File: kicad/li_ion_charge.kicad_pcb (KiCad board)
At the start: 2 copper layers, 18 parts, among them P101 USB_B, P102 CONN_01X02, P103 CONN_01X02, U101 MCP73834-FCI/UN

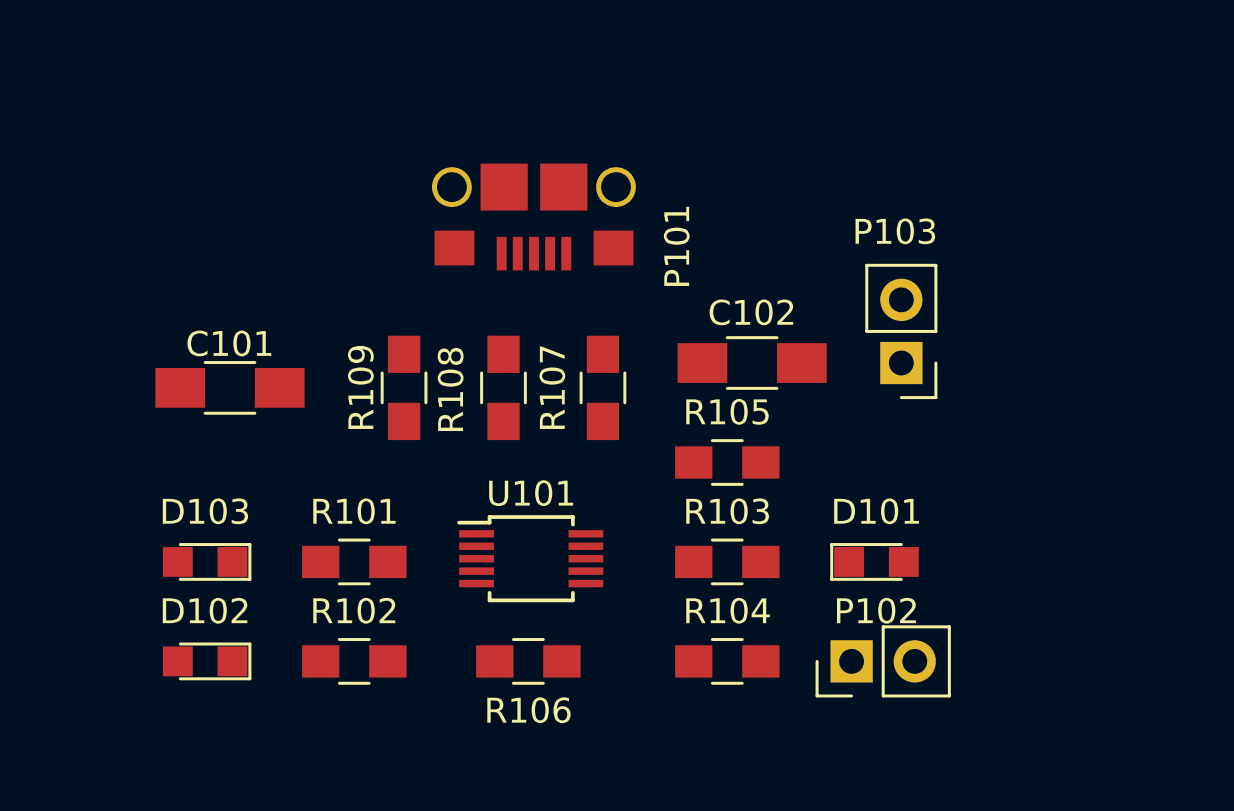
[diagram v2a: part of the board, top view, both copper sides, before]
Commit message: First iteration of adding power planes and initial traces. Still need to add osh-park defaults and address ERC errors
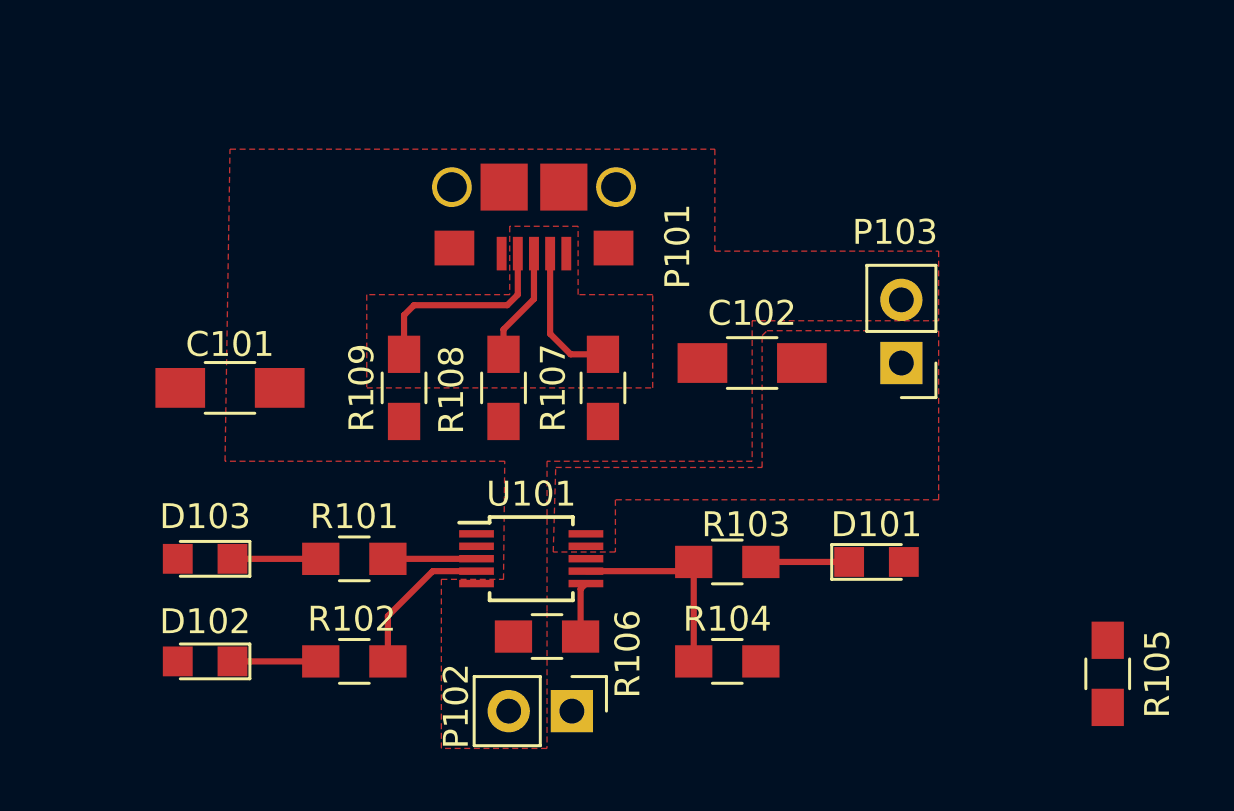
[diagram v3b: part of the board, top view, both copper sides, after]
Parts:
- moved R105 17.5 mm to (181.3, 107.5), turned to 270 degrees
- moved P102 11.4 mm to (159.8, 109.0), turned to 270 degrees
- moved R106 1.25 mm to (158.8, 106.0)
- moved D103 0.12 mm to (145.0, 102.9)
- moved R101 0.12 mm to (151.0, 102.9)
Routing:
- net /~TE: track 0.00 -> 8.49 mm
- net Net-(P101-Pad4): track 0.00 -> 8.14 mm
- net /Stat2: track 0.00 -> 6.14 mm
- net Net-(P101-Pad2): track 0.00 -> 5.69 mm
- net Net-(P101-Pad3): track 0.00 -> 4.56 mm
- net /Stat1: track 0.00 -> 3.57 mm
- net Net-(D103-Pad1): track 0.00 -> 3.55 mm
- net Net-(D102-Pad1): track 0.00 -> 3.55 mm
- net Net-(D101-Pad1): track 0.00 -> 3.55 mm
- net /Prog: track 0.00 -> 2.22 mm
- added copper zone on F.Cu, net /VBAT
- added copper zone on F.Cu, net GND
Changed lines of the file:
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@@
   (general
     (links 38)
-    (no_connects 38)
+    (no_connects 10)
     (area 0 0 0 0)
     (thickness 1.6)
     (drawings 0)
-    (tracks 2)
+    (tracks 26)
     (zones 0)
     (modules 18)
@@
     (last_trace_width 0.25)
     (trace_clearance 0.2)
-    (zone_clearance 0.508)
+    (zone_clearance 0.2032)
     (zone_45_only no)
     (trace_min 0.2)
@@
     (tags "LED led 0805 SMD smd SMT smt smdled SMDLED smtled SMTLED")
     (attr smd)
-    (fp_text reference D101 (at 0 -2) (layer F.SilkS)
+    (fp_text reference D101 (at 0 -1.5) (layer F.SilkS)
       (effects (font (size 1 1) (thickness 0.15)))
     )
@@
     (tags "LED led 0805 SMD smd SMT smt smdled SMDLED smtled SMTLED")
     (attr smd)
-    (fp_text reference D102 (at 0 2 180) (layer F.SilkS)
+    (fp_text reference D102 (at 0 1.6 180) (layer F.SilkS)
       (effects (font (size 1 1) (thickness 0.15)))
     )
@@
   )
   (module LEDs:LED_0805 (layer F.Cu)
-    (at 145 103 180)
+    (at 145 102.875 180)
     (descr "LED 0805 smd package")
     (tags "LED led 0805 SMD smd SMT smt smdled SMDLED smtled SMTLED")
     (attr smd)
-    (fp_text reference D103 (at 0 2 180) (layer F.SilkS)
+    (fp_text reference D103 (at 0 1.7 180) (layer F.SilkS)
       (effects (font (size 1 1) (thickness 0.15)))
     )
@@
   )
   (module Resistors_SMD:R_0805_HandSoldering (layer F.Cu)
-    (at 151 103 180)
+    (at 151 102.875 180)
     (descr "Resistor SMD 0805, hand soldering")
     (tags "resistor 0805")
     (attr smd)
-    (fp_text reference R101 (at 0 2 180) (layer F.SilkS)
+    (fp_text reference R101 (at 0 1.7 180) (layer F.SilkS)
       (effects (font (size 1 1) (thickness 0.15)))
     )
@@
     (tags "resistor 0805")
     (attr smd)
-    (fp_text reference R102 (at 0 2 180) (layer F.SilkS)
+    (fp_text reference R102 (at 0.1 1.7 180) (layer F.SilkS)
       (effects (font (size 1 1) (thickness 0.15)))
     )
@@
     (tags "resistor 0805")
     (attr smd)
-    (fp_text reference R103 (at 0 -2) (layer F.SilkS)
+    (fp_text reference R103 (at 0.75 -1.5) (layer F.SilkS)
       (effects (font (size 1 1) (thickness 0.15)))
     )
@@
     (tags "resistor 0805")
     (attr smd)
-    (fp_text reference R104 (at 0 -2) (layer F.SilkS)
+    (fp_text reference R104 (at 0 -1.7) (layer F.SilkS)
       (effects (font (size 1 1) (thickness 0.15)))
     )
@@
   )
   (module Resistors_SMD:R_0805_HandSoldering (layer F.Cu)
-    (at 166 99 180)
+    (at 181.3 107.5 270)
     (descr "Resistor SMD 0805, hand soldering")
     (tags "resistor 0805")
     (attr smd)
-    (fp_text reference R105 (at 0 2 180) (layer F.SilkS)
-      (effects (font (size 1 1) (thickness 0.15)))
-    )
-    (fp_text value 10k (at -4 0 180) (layer F.Fab)
-      (effects (font (size 1 1) (thickness 0.15)))
-    )
-    (fp_text user %R (at 0 -1.7 180) (layer F.Fab) hide
+    (fp_text reference R105 (at 0 -2 270) (layer F.SilkS)
+      (effects (font (size 1 1) (thickness 0.15)))
+    )
+    (fp_text value 10k (at -4 0 270) (layer F.Fab)
+      (effects (font (size 1 1) (thickness 0.15)))
+    )
+    (fp_text user %R (at 0 -1.7 270) (layer F.Fab) hide
       (effects (font (size 1 1) (thickness 0.15)))
     )
@@
     (fp_line (start 2.35 0.9) (end 2.35 -0.9) (layer F.CrtYd) (width 0.05))
     (fp_line (start 2.35 0.9) (end -2.35 0.9) (layer F.CrtYd) (width 0.05))
-    (pad 1 smd rect (at -1.35 0 180) (size 1.5 1.3) (layers F.Cu F.Paste F.Mask)
-      (net 1 GND))
-    (pad 2 smd rect (at 1.35 0 180) (size 1.5 1.3) (layers F.Cu F.Paste F.Mask)
+    (pad 1 smd rect (at -1.35 0 270) (size 1.5 1.3) (layers F.Cu F.Paste F.Mask)
+      (net 1 GND))
+    (pad 2 smd rect (at 1.35 0 270) (size 1.5 1.3) (layers F.Cu F.Paste F.Mask)
       (net 11 /Ther))
     (model Resistors_SMD.3dshapes/R_0805.wrl
@@
   )
   (module Resistors_SMD:R_0805_HandSoldering (layer F.Cu)
-    (at 158 107)
+    (at 158.75 106)
     (descr "Resistor SMD 0805, hand soldering")
     (tags "resistor 0805")
     (attr smd)
-    (fp_text reference R106 (at 0 2) (layer F.SilkS)
-      (effects (font (size 1 1) (thickness 0.15)))
-    )
-    (fp_text value 2k (at 3 0) (layer F.Fab)
+    (fp_text reference R106 (at 3.25 0.7 90) (layer F.SilkS)
+      (effects (font (size 1 1) (thickness 0.15)))
+    )
+    (fp_text value 2k (at 3 0) (layer F.Fab) hide
       (effects (font (size 1 1) (thickness 0.15)))
     )
@@
   )
   (module Pin_Headers:Pin_Header_Straight_1x02_Pitch2.54mm (layer F.Cu)
-    (at 171 107 90)
+    (at 159.75 109 270)
     (descr "Through hole straight pin header, 1x02, 2.54mm pitch, single row")
     (tags "Through hole pin header THT 1x02 2.54mm single row")
-    (fp_text reference P102 (at 2 1 180) (layer F.SilkS)
-      (effects (font (size 1 1) (thickness 0.15)))
-    )
-    (fp_text value CONN_01X02 (at 0 4.93 90) (layer F.Fab) hide
+    (fp_text reference P102 (at -0.2 4.65 270) (layer F.SilkS)
+      (effects (font (size 1 1) (thickness 0.15)))
+    )
+    (fp_text value CONN_01X02 (at 0 4.93 270) (layer F.Fab) hide
       (effects (font (size 1 1) (thickness 0.15)))
     )
@@
     (fp_line (start 1.6 4.1) (end 1.6 -1.6) (layer F.CrtYd) (width 0.05))
     (fp_line (start 1.6 -1.6) (end -1.6 -1.6) (layer F.CrtYd) (width 0.05))
-    (pad 1 thru_hole rect (at 0 0 90) (size 1.7 1.7) (drill 1) (layers *.Cu *.Mask)
+    (pad 1 thru_hole rect (at 0 0 270) (size 1.7 1.7) (drill 1) (layers *.Cu *.Mask)
       (net 9 /RESET))
-    (pad 2 thru_hole oval (at 0 2.54 90) (size 1.7 1.7) (drill 1) (layers *.Cu *.Mask)
+    (pad 2 thru_hole oval (at 0 2.54 270) (size 1.7 1.7) (drill 1) (layers *.Cu *.Mask)
       (net 1 GND))
     (model Pin_Headers.3dshapes/Pin_Header_Straight_1x02_Pitch2.54mm.wrl
@@
   (segment (start 86.3396 44.0503) (end 86.3396 44.7396) (width 0.25) (layer F.Cu) (net 0))
   (segment (start 96.6 58.05) (end 96.4 58.25) (width 0.25) (layer F.Cu) (net 0))
+  (segment (start 167.35 103) (end 170.9 103) (width 0.25) (layer F.Cu) (net 2) (status C00000))
+  (segment (start 146.1 107) (end 149.65 107) (width 0.25) (layer F.Cu) (net 3) (status C00000))
+  (segment (start 146.1 102.875) (end 149.65 102.875) (width 0.25) (layer F.Cu) (net 4) (status C00000))
+  (segment (start 158.225 90.6) (end 158.225 92.425) (width 0.25) (layer F.Cu) (net 5) (status 400000))
+  (segment (start 157 93.65) (end 157 94.65) (width 0.25) (layer F.Cu) (net 5) (status 800000))
+  (segment (start 158.225 92.425) (end 157 93.65) (width 0.25) (layer F.Cu) (net 5))
+  (segment (start 158.875 90.6) (end 158.875 93.825) (width 0.25) (layer F.Cu) (net 6) (status 400000))
+  (segment (start 159.7 94.65) (end 161 94.65) (width 0.25) (layer F.Cu) (net 6) (status 800000))
+  (segment (start 158.875 93.825) (end 159.7 94.65) (width 0.25) (layer F.Cu) (net 6))
+  (segment (start 164.65 107) (end 164.65 103) (width 0.25) (layer F.Cu) (net 10) (status C00000))
+  (segment (start 164.65 103) (end 164.28 103.37) (width 0.25) (layer F.Cu) (net 10) (status C00000))
+  (segment (start 164.28 103.37) (end 160.315 103.37) (width 0.25) (layer F.Cu) (net 10) (status C00000))
+  (segment (start 160.1 106) (end 160.1 104.085) (width 0.25) (layer F.Cu) (net 12) (status 400000))
+  (segment (start 160.1 104.085) (end 160.315 103.87) (width 0.25) (layer F.Cu) (net 12) (status 800000))
+  (segment (start 152.35 102.875) (end 155.91 102.875) (width 0.25) (layer F.Cu) (net 13))
+  (segment (start 155.91 102.875) (end 155.915 102.87) (width 0.25) (layer F.Cu) (net 13))
+  (segment (start 155.915 103.37) (end 154.155 103.37) (width 0.25) (layer F.Cu) (net 14) (status 400000))
+  (segment (start 152.35 105.175) (end 152.35 107) (width 0.25) (layer F.Cu) (net 14) (status 800000))
+  (segment (start 154.155 103.37) (end 152.35 105.175) (width 0.25) (layer F.Cu) (net 14))
+  (segment (start 157.575 90.6) (end 157.575 92.25) (width 0.25) (layer F.Cu) (net 15) (status 400000))
+  (segment (start 153 93.075) (end 153 94.65) (width 0.25) (layer F.Cu) (net 15) (status 800000))
+  (segment (start 153.4 92.675) (end 153 93.075) (width 0.25) (layer F.Cu) (net 15))
+  (segment (start 157.15 92.675) (end 153.4 92.675) (width 0.25) (layer F.Cu) (net 15))
+  (segment (start 157.575 92.25) (end 157.15 92.675) (width 0.25) (layer F.Cu) (net 15))
+  (zone (net 1) (net_name GND) (layer F.Cu) (hatch edge 0.508)
+    (connect_pads (clearance 0.2032))
+    (min_thickness 0.254)
+    (fill yes (arc_segments 16) (thermal_gap 0.254) (thermal_bridge_width 0.508))
+    (polygon
+      (pts
+        (xy 165.5 90.5) (xy 174.5 90.5) (xy 174.5 93.3) (xy 167 93.3) (xy 167 97)
+        (xy 167 98.95) (xy 158.75 98.95) (xy 158.75 105) (xy 158.75 110.5) (xy 154.5 110.5)
+        (xy 154.5 103.7) (xy 157 103.7) (xy 157.05 98.95) (xy 145.8 98.95) (xy 146 86.4)
+        (xy 165.5 86.4)
+      )
+    )
+    (polygon
+      (pts        (xy 157.25 89.5) (xy 157.25 92.25) (xy 151.5 92.25) (xy 151.5 96) (xy 163 96)
+        (xy 163 92.25) (xy 160 92.25) (xy 160 89.5)
+      )
+    )
+  )
+  (zone (net 7) (net_name /VBAT) (layer F.Cu) (hatch edge 0.508)
+    (connect_pads (clearance 0.2032))
+    (min_thickness 0.254)
+    (fill yes (arc_segments 16) (thermal_gap 0.254) (thermal_bridge_width 0.508))
+    (polygon
+      (pts
+        (xy 167.6 93.7) (xy 174.5 93.7) (xy 174.5 100.5) (xy 161.5 100.5) (xy 161.5 102.6)
+        (xy 159 102.6) (xy 159.1 99.2) (xy 167.4 99.2) (xy 167.4 93.9)
+      )
+    )
+  )
 )
